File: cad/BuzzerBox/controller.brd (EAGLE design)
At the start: 100 x 100 mm, 130 parts, among them J1 USB_A_SMT_FEMALE, Q1 BSS138, Q2 BSS138, Q3 BSS138, T1 BC849, T10 BC849, T2 BC849, T3 BC849, T4 BC849, T5 BC849, T6 BC849, T7 BC849, T8 BC849, T9 BC849, U1 ATMEGA328P-AU, Y1 16MHz

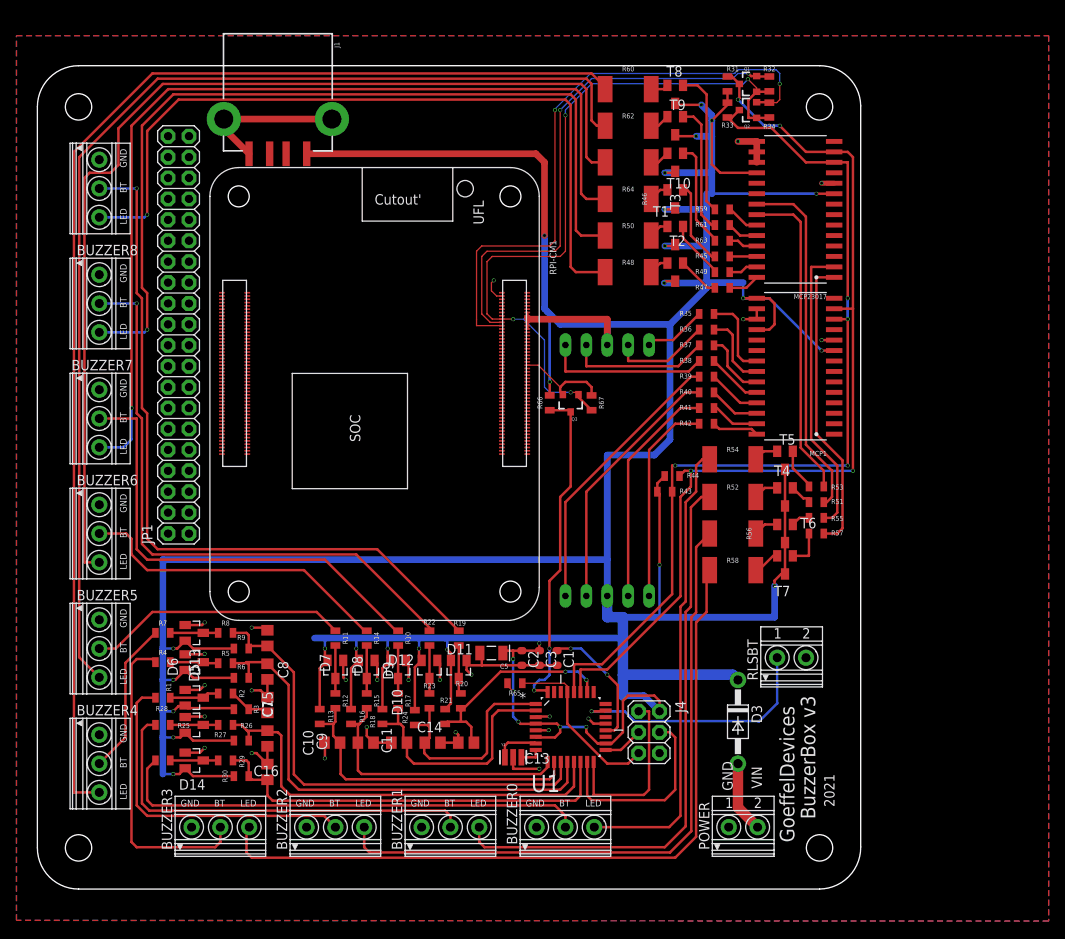
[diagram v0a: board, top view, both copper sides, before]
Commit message: Added HDMI
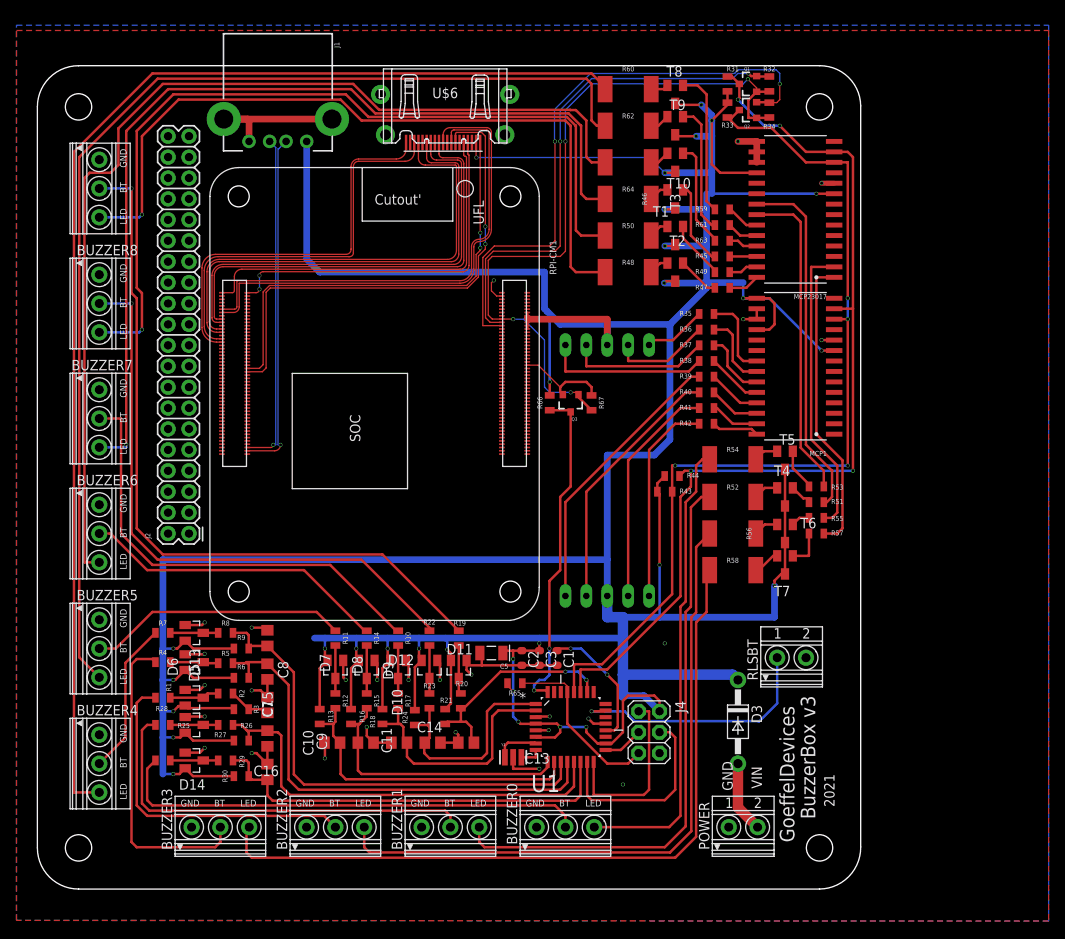
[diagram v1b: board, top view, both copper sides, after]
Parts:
- removed JP1: (no value), pinhead:2X20
- added J2: RASPBERRYPI-40-PIN-GPIO_PTH_NO_SHROUD, Custom-Connector:2X20
- added U$6: HDMI-A, connectors:HDMI_A
- J1: device SparkFun-Connectors:USB-A-S-SILK-FEMALE -> Custom-Connector:USB-A-S-SILK-FEMALE
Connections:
- new net HDMI_CEC: RPI-CM1.151, U$6.P$13
- new net HDMI_CLK_N: RPI-CM1.190, U$6.P$12
- new net HDMI_CLK_P: RPI-CM1.188, U$6.P$10
- new net HDMI_D0_N: RPI-CM1.184, U$6.P$9
- new net HDMI_D0_P: RPI-CM1.182, U$6.P$7
- new net HDMI_D1_N: RPI-CM1.178, U$6.P$6
- new net HDMI_D1_P: RPI-CM1.176, U$6.P$4
- new net HDMI_D2_N: RPI-CM1.172, U$6.P$3
- new net HDMI_D2_P: RPI-CM1.170, U$6.P$1
- new net HDMI_HOT: RPI-CM1.153, U$6.P$19
- new net HDMI_SCL: RPI-CM1.200, U$6.P$15
- new net HDMI_SDA: RPI-CM1.199, U$6.P$16
- net +3V3: now also J2.1, J2.17
- net +5V: now also J2.2, J2.4, U$6.P$18
- net GND: now also J2.14, J2.20, J2.25, J2.30, J2.34, J2.39, J2.6, J2.9, RPI-CM1.107, RPI-CM1.108, RPI-CM1.113, RPI-CM1.114, RPI-CM1.119, RPI-CM1.120, RPI-CM1.125, RPI-CM1.126, RPI-CM1.131, RPI-CM1.132, RPI-CM1.137, RPI-CM1.138, RPI-CM1.144, RPI-CM1.150, RPI-CM1.155, RPI-CM1.156, RPI-CM1.161, RPI-CM1.162, RPI-CM1.167, RPI-CM1.168, RPI-CM1.173, RPI-CM1.174, RPI-CM1.179, RPI-CM1.180, RPI-CM1.185, RPI-CM1.186, RPI-CM1.191, RPI-CM1.192, RPI-CM1.197, RPI-CM1.198
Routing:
- net HDMI_CEC: track 0.00 -> 60.7 mm, vias 0 -> 2
- net HDMI_CLK_P: track 0.00 -> 59.4 mm
- net HDMI_CLK_N: track 0.00 -> 57.7 mm
- net HDMI_D1_P: track 0.00 -> 57.0 mm
- net HDMI_D1_N: track 0.00 -> 56.0 mm
- net HDMI_D0_P: track 0.00 -> 54.7 mm
- net HDMI_HOT: track 0.00 -> 54.0 mm, vias 0 -> 2
- net HDMI_D0_N: track 0.00 -> 53.7 mm
- net HDMI_D2_N: track 0.00 -> 48.3 mm
- net HDMI_D2_P: track 0.00 -> 47.9 mm
- net HDMI_SCL: track 0.00 -> 46.9 mm
- net HDMI_SDA: track 0.00 -> 44.3 mm, vias 0 -> 2
- net USB_N: track 0.00 -> 42.0 mm, vias 0 -> 1
- net USB_P: track 0.00 -> 40.8 mm, vias 0 -> 1
- net +5V: track 597.3 -> 624.0 mm
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
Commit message: Add pin header to support external PI
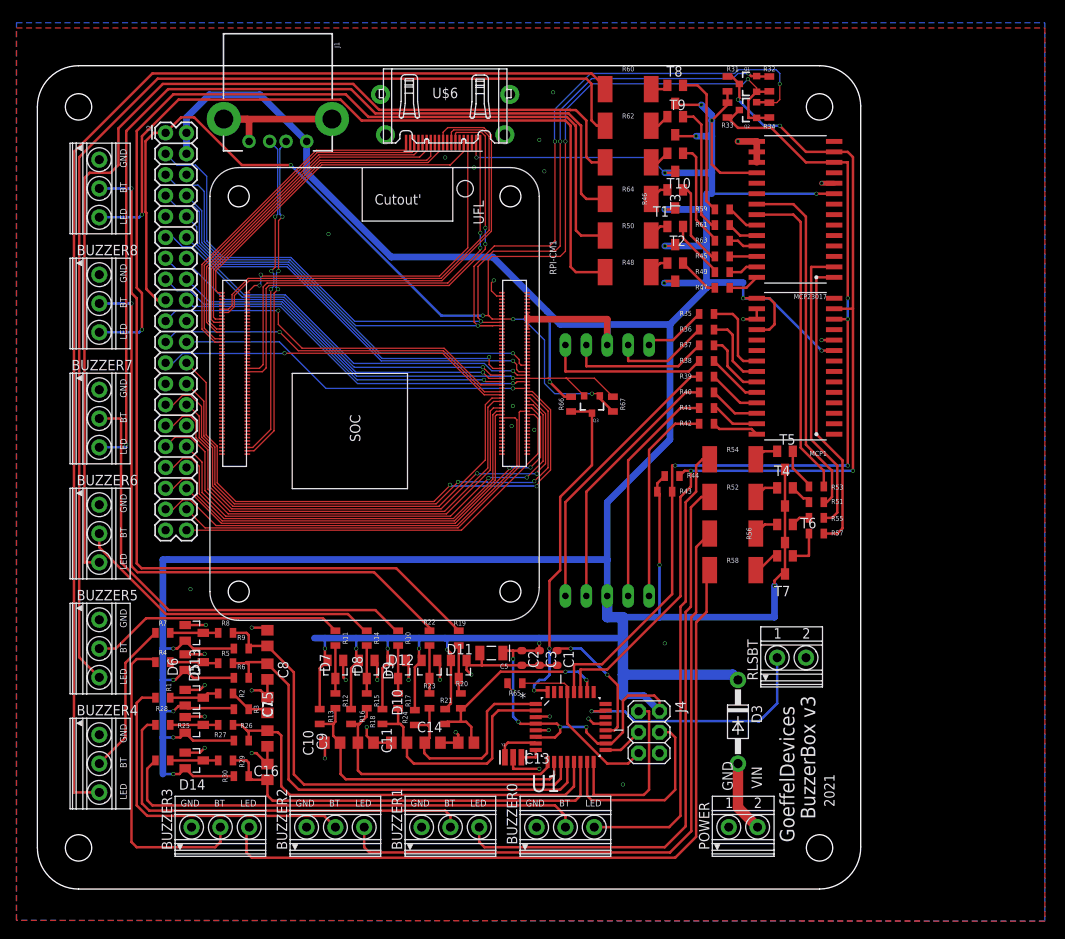
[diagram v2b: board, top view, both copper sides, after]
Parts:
- moved J2 48.7 mm to (15.6, 91.8), turned to 270 degrees
- moved R66 2.60 mm to (64.8, 58.9)
- moved Q3 2.60 mm to (67.4, 58.9)
- moved R67 2.60 mm to (69.9, 58.9)
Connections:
- removed net N$41: Q1.2, R32.1, RPI-CM1.82
- removed net N$47: Q3.2, R67.1, RPI-CM1.55
- new net GP10: J2.19, RPI-CM1.44
- new net GP11: J2.23, RPI-CM1.38
- new net GP12: J2.32, RPI-CM1.31
- new net GP13: J2.33, RPI-CM1.28
- new net GP14: J2.8, RPI-CM1.55
- new net GP15: J2.10, RPI-CM1.51
- new net GP16: J2.36, RPI-CM1.29
- new net GP17: J2.11, RPI-CM1.50
- new net GP18: J2.12, RPI-CM1.49
- new net GP19: J2.35, RPI-CM1.26
- new net GP2: RPI-CM1.58
- new net GP20: J2.38, RPI-CM1.27
- new net GP21: J2.40, RPI-CM1.25
- new net GP22: J2.15, RPI-CM1.46
- new net GP23: J2.16, Q3.2, R67.1, RPI-CM1.47
- new net GP24: J2.18, RPI-CM1.45
- new net GP25: J2.22, RPI-CM1.41
- new net GP26: J2.37, RPI-CM1.24
- new net GP27: J2.13, RPI-CM1.48
- new net GP3: RPI-CM1.56
- new net GP4: J2.7, RPI-CM1.54
- new net GP5: J2.29, RPI-CM1.34
- new net GP6: J2.31, RPI-CM1.30
- new net GP7: J2.26, RPI-CM1.37
- new net GP8: J2.24, RPI-CM1.39
- new net GP9: J2.21, RPI-CM1.40
- new net ID_SC: J2.28, RPI-CM1.35
- new net ID_SD: J2.27, RPI-CM1.36
- new net SDAPI: J2.3, Q1.2, R32.1, RPI-CM1.82
- net GND: now also U$6.P$11, U$6.P$17, U$6.P$2, U$6.P$5, U$6.P$8
- net SCLPI: now also J2.5
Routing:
- net SDAPI: track 0.00 -> 115.7 mm, vias 0 -> 3
- net +3V3: track 87.9 -> 164.0 mm, vias 4 -> 6
- net GP8: track 0.00 -> 70.6 mm, vias 0 -> 2
- net GP7: track 0.00 -> 67.2 mm, vias 0 -> 2
- net ID_SC: track 0.00 -> 64.6 mm, vias 0 -> 2
- net N$41: track 63.0 -> 0.00 mm, vias 2 -> 0
- net ID_SD: track 0.00 -> 61.1 mm
- net GP23: track 0.00 -> 60.7 mm, vias 0 -> 1
- net GP5: track 0.00 -> 59.9 mm
- net GP12: track 0.00 -> 59.8 mm, vias 0 -> 2
- net GP6: track 0.00 -> 57.5 mm
- net GP13: track 0.00 -> 56.3 mm
- net GP16: track 0.00 -> 55.2 mm, vias 0 -> 2
- net GP26: track 0.00 -> 55.0 mm
- net GP19: track 0.00 -> 54.1 mm
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
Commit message: Add slots to HDMI port
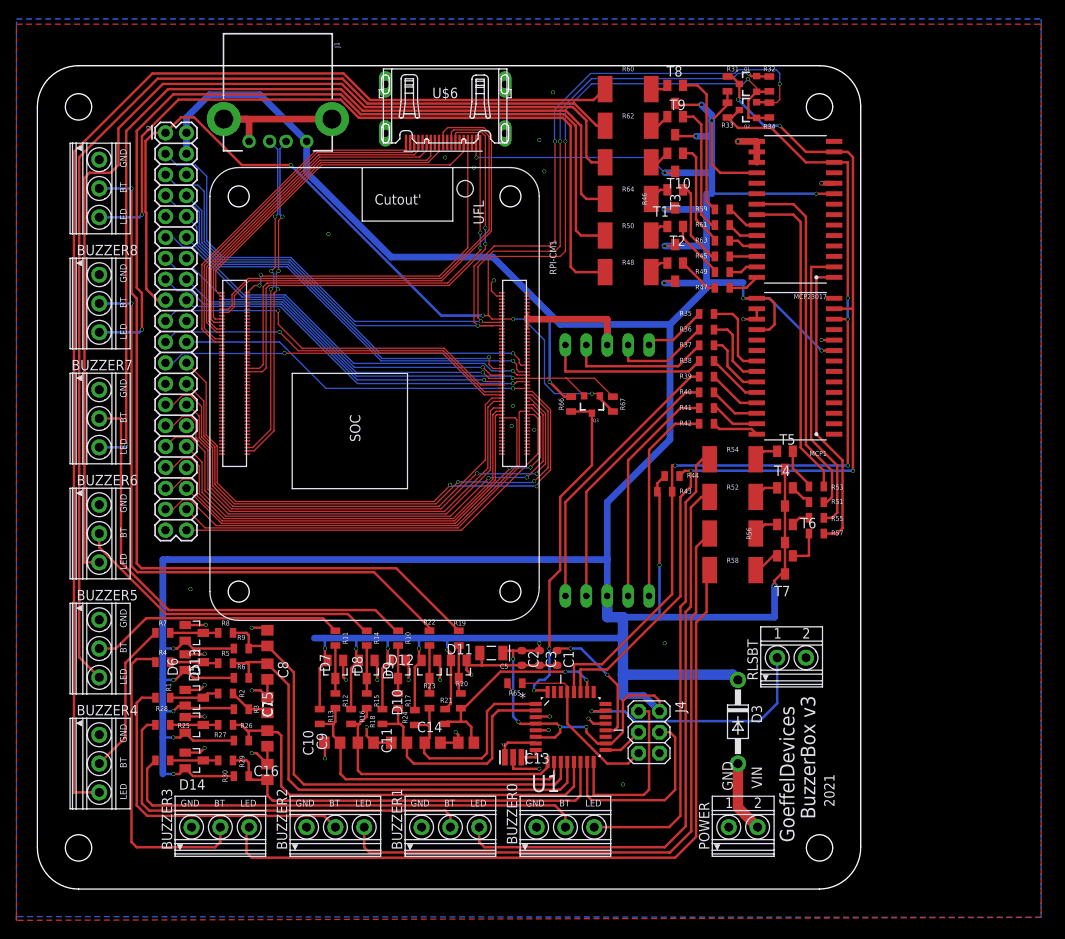
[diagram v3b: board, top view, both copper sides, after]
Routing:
- net LED0A3: track 137.0 -> 134.4 mm
- net LED0A2: track 150.3 -> 151.5 mm
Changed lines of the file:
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@@
 <polygon width="0.127" layer="1" isolate="0.2032">
 <vertex x="-2.54" y="-3.80158125"/>
-<vertex x="-2.54" y="104.5848"/>
-<vertex x="122.3678" y="104.5848"/>
-<vertex x="122.3678" y="-3.897759375"/>
+<vertex x="-2.54" y="-3.344734375"/>
+<vertex x="-2.54" y="105.042"/>
+<vertex x="121.9106" y="105.042"/>
+<vertex x="121.9106" y="-3.440559375"/>
 </polygon>
 <contactref element="RLSBT" pad="2"/>
@@
 <wire x1="22.64" y1="93.52" x2="35.78" y2="93.52" width="0.8128" layer="1"/>
 <polygon width="0.127" layer="16" isolate="0.2032">
+<vertex x="-2.54" y="-3.344734375"/>
 <vertex x="-2.54" y="-3.80158125"/>
-<vertex x="-2.54" y="105.2198"/>
-<vertex x="122.3678" y="105.2198"/>
-<vertex x="122.3678" y="-3.897759375"/>
+<vertex x="-2.54" y="105.677"/>
+<vertex x="121.9106" y="105.677"/>
+<vertex x="121.9106" y="-3.440559375"/>
 </polygon>
 <via x="76.2" y="29.845" extent="1-16" drill="0.35"/>
@@
 <contactref element="R60" pad="1"/>
 <wire x1="4.445" y1="11.74" x2="7.52" y2="11.74" width="0.3048" layer="1"/>
-<wire x1="68.955" y1="97.155" x2="68.955" y2="97.415" width="0.3048" layer="1"/>
-<wire x1="68.955" y1="97.415" x2="67.31" y2="99.06" width="0.3048" layer="1"/>
-<wire x1="67.31" y1="99.06" x2="13.97" y2="99.06" width="0.3048" layer="1"/>
+<wire x1="68.955" y1="97.155" x2="68.955" y2="97.2312" width="0.3048" layer="1"/>
+<wire x1="68.955" y1="97.2312" x2="68.955" y2="97.415" width="0.3048" layer="1"/>
+<wire x1="37.1856" y1="99.06" x2="13.97" y2="99.06" width="0.3048" layer="1"/>
 <wire x1="13.97" y1="99.06" x2="4.445" y2="89.535" width="0.3048" layer="1"/>
 <wire x1="4.445" y1="89.535" x2="4.445" y2="11.74" width="0.3048" layer="1"/>
+<wire x1="37.1856" y1="99.06" x2="40.4114" y2="95.8342" width="0.3048" layer="1"/>
+<wire x1="67.558" y1="95.8342" x2="68.955" y2="97.2312" width="0.3048" layer="1"/>
+<wire x1="40.4114" y1="95.8342" x2="67.558" y2="95.8342" width="0.3048" layer="1"/>
 </signal>
 <signal name="LED0A3">
@@
 <wire x1="5.08" y1="88.9" x2="5.08" y2="28.15" width="0.3048" layer="1"/>
 <wire x1="7.52" y1="25.71" x2="5.08" y2="28.15" width="0.3048" layer="1"/>
-<wire x1="67.945" y1="92.71" x2="68.955" y2="92.71" width="0.3048" layer="1"/>
-<wire x1="67.31" y1="97.79" x2="67.31" y2="93.345" width="0.3048" layer="1"/>
-<wire x1="67.31" y1="97.79" x2="66.675" y2="98.425" width="0.3048" layer="1"/>
-<wire x1="66.675" y1="98.425" x2="14.605" y2="98.425" width="0.3048" layer="1"/>
-<wire x1="14.605" y1="98.425" x2="5.08" y2="88.9" width="0.3048" layer="1"/>
-<wire x1="67.31" y1="93.345" x2="67.945" y2="92.71" width="0.3048" layer="1"/>
+<wire x1="5.08" y1="88.9" x2="14.605" y2="98.425" width="0.3048" layer="1"/>
+<wire x1="40.0812" y1="95.4024" x2="65.2282625" y2="95.4024" width="0.3048" layer="1"/>
+<wire x1="65.2282625" y1="95.4024" x2="67.9206625" y2="92.71" width="0.3048" layer="1"/>
+<wire x1="14.605" y1="98.425" x2="37.0586" y2="98.425" width="0.3048" layer="1"/>
+<wire x1="37.0586" y1="98.425" x2="40.0812" y2="95.4024" width="0.3048" layer="1"/>
+<wire x1="67.9206625" y1="92.71" x2="68.955" y2="92.71" width="0.3048" layer="1"/>
 </signal>
 <signal name="LED0A4">
@@
 <wire x1="67.31" y1="88.265" x2="68.955" y2="88.265" width="0.3048" layer="1"/>
 <wire x1="66.675" y1="93.345" x2="66.675" y2="88.9" width="0.3048" layer="1"/>
-<wire x1="38.3552375" y1="97.79" x2="15.24" y2="97.79" width="0.3048" layer="1"/>
+<wire x1="36.9836375" y1="97.79" x2="15.24" y2="97.79" width="0.3048" layer="1"/>
 <wire x1="5.715" y1="86.36" x2="5.715" y2="39.68" width="0.3048" layer="1"/>
 <wire x1="7.52" y1="39.68" x2="5.715" y2="39.68" width="0.3048" layer="1"/>
@@
 <wire x1="6.35" y1="86.995" x2="5.715" y2="86.36" width="0.3048" layer="1"/>
 <wire x1="66.675" y1="88.9" x2="67.31" y2="88.265" width="0.3048" layer="1"/>
-<wire x1="38.3552375" y1="97.79" x2="41.5048375" y2="94.6404" width="0.3048" layer="1"/>
-<wire x1="64.695925" y1="94.6404" x2="64.721325" y2="94.615" width="0.3048" layer="1"/>
-<wire x1="64.721325" y1="94.615" x2="65.405" y2="94.615" width="0.3048" layer="1"/>
-<wire x1="41.5048375" y1="94.6404" x2="64.695925" y2="94.6404" width="0.3048" layer="1"/>
-<wire x1="65.405" y1="94.615" x2="66.675" y2="93.345" width="0.3048" layer="1"/>
+<wire x1="36.9836375" y1="97.79" x2="39.8030375" y2="94.9706" width="0.3048" layer="1"/>
+<wire x1="65.0494" y1="94.9706" x2="66.675" y2="93.345" width="0.3048" layer="1"/>
+<wire x1="39.8030375" y1="94.9706" x2="65.0494" y2="94.9706" width="0.3048" layer="1"/>
 </signal>
 <signal name="LED1A5">
@@
 <wire x1="66.675" y1="83.82" x2="68.955" y2="83.82" width="0.3048" layer="1"/>
 <wire x1="66.04" y1="92.71" x2="66.04" y2="84.455" width="0.3048" layer="1"/>
-<wire x1="15.875" y1="97.155" x2="38.1" y2="97.155" width="0.3048" layer="1"/>
+<wire x1="15.875" y1="97.155" x2="36.8808" y2="97.155" width="0.3048" layer="1"/>
 <wire x1="15.875" y1="97.155" x2="10.795" y2="92.075" width="0.3048" layer="1"/>
 <wire x1="10.795" y1="92.075" x2="10.795" y2="53.975" width="0.3048" layer="1"/>
@@
 <wire x1="66.04" y1="84.455" x2="66.675" y2="83.82" width="0.3048" layer="1"/>
 <wire x1="66.0156625" y1="92.71" x2="66.04" y2="92.71" width="0.3048" layer="1"/>
-<wire x1="41.0464" y1="94.2086" x2="64.5170625" y2="94.2086" width="0.3048" layer="1"/>
-<wire x1="64.5170625" y1="94.2086" x2="66.0156625" y2="92.71" width="0.3048" layer="1"/>
-<wire x1="38.1" y1="97.155" x2="41.0464" y2="94.2086" width="0.3048" layer="1"/>
+<wire x1="39.497" y1="94.5388" x2="64.1868625" y2="94.5388" width="0.3048" layer="1"/>
+<wire x1="64.1868625" y1="94.5388" x2="66.0156625" y2="92.71" width="0.3048" layer="1"/>
+<wire x1="36.8808" y1="97.155" x2="39.497" y2="94.5388" width="0.3048" layer="1"/>
 </signal>
 <signal name="LED1A7">
@@
 <wire x1="64.77" y1="75.565" x2="65.405" y2="74.93" width="0.3048" layer="1"/>
 <contactref element="BUZZER9" pad="3"/>
-<wire x1="36.83" y1="95.885" x2="39.37" y2="93.345" width="0.3048" layer="1"/>
-<wire x1="64.135" y1="93.345" x2="64.77" y2="92.71" width="0.3048" layer="1"/>
-<wire x1="39.37" y1="93.345" x2="64.135" y2="93.345" width="0.3048" layer="1"/>
+<wire x1="36.83" y1="95.885" x2="39.0398" y2="93.6752" width="0.3048" layer="1"/>
+<wire x1="63.8048" y1="93.6752" x2="64.77" y2="92.71" width="0.3048" layer="1"/>
+<wire x1="63.8048" y1="93.6752" x2="39.0398" y2="93.6752" width="0.3048" layer="1"/>
 </signal>
 <signal name="LED1A6">
@@
 <wire x1="12.7" y1="67.945" x2="12.375" y2="67.62" width="0.3048" layer="16"/>
 <wire x1="12.375" y1="67.62" x2="7.52" y2="67.62" width="0.3048" layer="16"/>
-<wire x1="16.51" y1="96.52" x2="37.465" y2="96.52" width="0.3048" layer="1"/>
+<wire x1="16.51" y1="96.52" x2="36.8554" y2="96.52" width="0.3048" layer="1"/>
 <wire x1="65.405" y1="80.01" x2="66.04" y2="79.375" width="0.3048" layer="1"/>
 <wire x1="12.7" y1="67.945" x2="12.7" y2="72.39" width="0.3048" layer="1"/>
@@
 <wire x1="12.065" y1="73.025" x2="12.065" y2="92.075" width="0.3048" layer="1"/>
 <wire x1="12.065" y1="92.075" x2="16.51" y2="96.52" width="0.3048" layer="1"/>
-<wire x1="40.2082" y1="93.7768" x2="64.3138625" y2="93.7768" width="0.3048" layer="1"/>
+<wire x1="39.2684" y1="94.107" x2="63.9836625" y2="94.107" width="0.3048" layer="1"/>
 <wire x1="65.3806625" y1="92.71" x2="65.405" y2="92.71" width="0.3048" layer="1"/>
-<wire x1="64.3138625" y1="93.7768" x2="65.3806625" y2="92.71" width="0.3048" layer="1"/>
-<wire x1="37.465" y1="96.52" x2="40.2082" y2="93.7768" width="0.3048" layer="1"/>
+<wire x1="63.9836625" y1="94.107" x2="65.3806625" y2="92.71" width="0.3048" layer="1"/>
+<wire x1="36.8554" y1="96.52" x2="39.2684" y2="94.107" width="0.3048" layer="1"/>
 </signal>
 <signal name="LED1A0">

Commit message: Organize Sikscreen
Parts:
- moved T7 0.30 mm to (90.8, 39.1)
- moved R13 0.15 mm to (34.3, 20.8)
- moved R16 0.15 mm to (38.1, 20.8)
- moved R18 0.15 mm to (41.9, 20.8)
- moved R21 0.15 mm to (49.5, 20.8)
- renumbered J1 to USB0, MCP23017 to MCP2, RPI-CM1 to RPI-CM4, U$6 to HDMI0
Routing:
- net +5V: track 636.1 -> 636.9 mm
